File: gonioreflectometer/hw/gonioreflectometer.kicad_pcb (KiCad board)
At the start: 2 copper layers, 25.8 x 20.3 mm, 39 parts, among them J1 Conn_01x07_Pin, J2 Conn_01x07_Pin, Q1 SS8050 200-350, Q10 AO3401A, Q2 SS8050 200-350, Q3 SS8050 200-350, Q4 AO3401A, Q5 AO3400A, Q6 AO3401A, Q7 AO3401A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

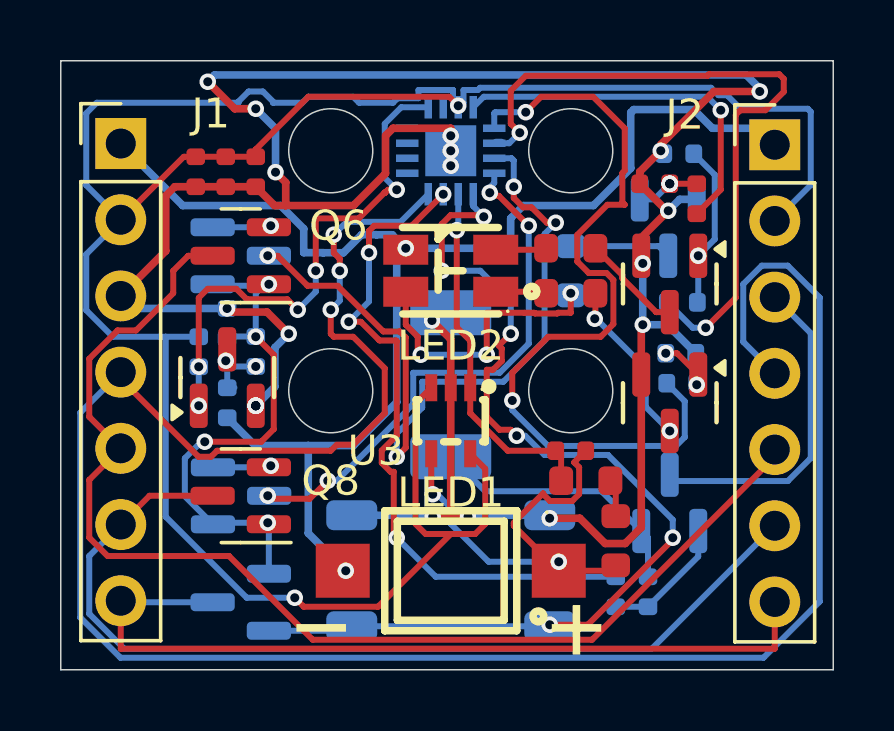
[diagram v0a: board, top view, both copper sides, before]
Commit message: v1.1 fix drc
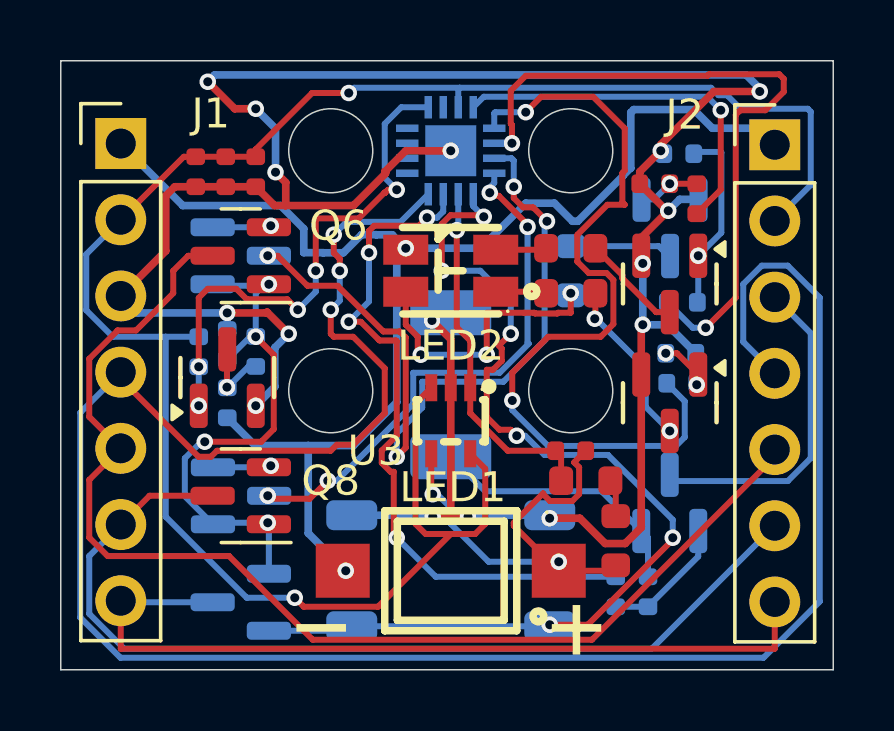
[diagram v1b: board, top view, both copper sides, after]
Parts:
- moved R15 0.70 mm to (75.5, 109.0)
- moved Q3 0.06 mm to (90.3, 105.1)
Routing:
- net 3.3v: track 83.0 -> 65.4 mm
- net GND: track 88.6 -> 87.0 mm, vias 20 -> 16
- net Net-(Q1-B): track 5.48 -> 6.28 mm
- net Net-(Q9-C): track 2.24 -> 2.51 mm, vias 2 -> 1
- net Net-(Q3-B): track 2.12 -> 2.06 mm, vias 2 -> 1

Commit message: v1.1 fix silkscreen on pad
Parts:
- moved R2 0.52 mm to (86.9, 107.8), turned to 15 degrees
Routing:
- net Net-(LED2---Pad3): track 9.38 -> 12.1 mm
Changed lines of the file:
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@@
 			(plot_on_all_layers_selection 0x00000000_00000000_00000000_00000000)
 			(disableapertmacros no)
-			(usegerberextensions no)
+			(usegerberextensions yes)
 			(usegerberattributes yes)
 			(usegerberadvancedattributes yes)
@@
 			(outputformat 1)
 			(mirror no)
-			(drillshape 1)
+			(drillshape 0)
 			(scaleselection 1)
-			(outputdirectory "")
+			(outputdirectory "gerber/")
 		)
 	)
@@
 	(footprint "PCM_JLCPCB:R_0603"
 		(layer "F.Cu")
-		(at 87 107.25)
+		(at 86.93 107.77 15)
 		(descr "Resistor SMD 0603 (1608 Metric), square (rectangular) end terminal, IPC_7351 nominal, (Body size source: IPC-SM-782 page 72, https://www.pcb-3d.com/wordpress/wp-content/uploads/ipc-sm-782a_amendment_1_and_2.pdf), generated with kicad-footprint-generator")
 		(tags "resistor")
 		(property "Reference" "R2"
-			(at 0 -1.3 0)
+			(at 0 -1.3 15)
 			(layer "F.SilkS")
 			(hide yes)
@@
 		)
 		(property "Value" "150Ω"
-			(at 0 1.43 0)
+			(at 0 1.43 15)
 			(layer "F.Fab")
 			(effects
@@
 		)
 		(property "Datasheet" "https://www.lcsc.com/datasheet/lcsc_datasheet_2206010130_UNI-ROYAL-Uniroyal-Elec-0603WAF1500T5E_C22808.pdf"
-			(at 0 0 0)
+			(at 0 0 15)
 			(unlocked yes)
 			(layer "F.Fab")
@@
 		)
 		(property "Description" "100mW Thick Film Resistors 75V ±100ppm/°C ±1% 150Ω 0603 Chip Resistor - Surface Mount ROHS"
-			(at 0 0 0)
+			(at 0 0 15)
 			(unlocked yes)
 			(layer "F.Fab")
@@
 		)
 		(property "LCSC" "C22808"
-			(at 0 0 0)
+			(at 0 0 15)
 			(unlocked yes)
 			(layer "F.Fab")
@@
 		)
 		(property "Stock" "598005"
-			(at 0 0 0)
+			(at 0 0 15)
 			(unlocked yes)
 			(layer "F.Fab")
@@
 		)
 		(property "Price" "0.004USD"
-			(at 0 0 0)
+			(at 0 0 15)
 			(unlocked yes)
 			(layer "F.Fab")
@@
 		)
 		(property "Process" "SMT"
-			(at 0 0 0)
+			(at 0 0 15)
 			(unlocked yes)
 			(layer "F.Fab")
@@
 		)
 		(property "Minimum Qty" "20"
-			(at 0 0 0)
+			(at 0 0 15)
 			(unlocked yes)
 			(layer "F.Fab")
@@
 		)
 		(property "Attrition Qty" "10"
-			(at 0 0 0)
+			(at 0 0 15)
 			(unlocked yes)
 			(layer "F.Fab")
@@
 		)
 		(property "Class" "Basic Component"
-			(at 0 0 0)
+			(at 0 0 15)
 			(unlocked yes)
 			(layer "F.Fab")
@@
 		)
 		(property "Category" "Resistors,Chip Resistor - Surface Mount"
-			(at 0 0 0)
+			(at 0 0 15)
 			(unlocked yes)
 			(layer "F.Fab")
@@
 		)
 		(property "Manufacturer" "UNI-ROYAL(Uniroyal Elec)"
-			(at 0 0 0)
+			(at 0 0 15)
 			(unlocked yes)
 			(layer "F.Fab")
@@
 		)
 		(property "Part" "0603WAF1500T5E"
-			(at 0 0 0)
+			(at 0 0 15)
 			(unlocked yes)
 			(layer "F.Fab")
@@
 		)
 		(property "Resistance" "150Ω"
-			(at 0 0 0)
+			(at 0 0 15)
 			(unlocked yes)
 			(layer "F.Fab")
@@
 		)
 		(property "Power(Watts)" "100mW"
-			(at 0 0 0)
+			(at 0 0 15)
 			(unlocked yes)
 			(layer "F.Fab")
@@
 		)
 		(property "Type" "Thick Film Resistors"
-			(at 0 0 0)
+			(at 0 0 15)
 			(unlocked yes)
 			(layer "F.Fab")
@@
 		)
 		(property "Overload Voltage (Max)" "75V"
-			(at 0 0 0)
+			(at 0 0 15)
 			(unlocked yes)
 			(layer "F.Fab")
@@
 		)
 		(property "Operating Temperature Range" "-55°C~+155°C"
-			(at 0 0 0)
+			(at 0 0 15)
 			(unlocked yes)
 			(layer "F.Fab")
@@
 		)
 		(property "Tolerance" "±1%"
-			(at 0 0 0)
+			(at 0 0 15)
 			(unlocked yes)
 			(layer "F.Fab")
@@
 		)
 		(property "Temperature Coefficient" "±100ppm/°C"
-			(at 0 0 0)
+			(at 0 0 15)
 			(unlocked yes)
 			(layer "F.Fab")
@@
 		)
 		(fp_text user "${REFERENCE}"
-			(at 0 0 0)
+			(at 0 0 15)
 			(layer "F.Fab")
 			(effects
@@
 		)
 		(pad "1" smd roundrect
-			(at -0.82 0)
+			(at -0.82 0 15)
 			(size 0.8 0.95)
 			(layers "F.Cu" "F.Mask" "F.Paste")
@@
 		)
 		(pad "2" smd roundrect
-			(at 0.82 0)
+			(at 0.82 0 15)
 			(size 0.8 0.95)
 			(layers "F.Cu" "F.Mask" "F.Paste")
@@
 	)
 	(segment
-		(start 86.13 107.2)
-		(end 86.18 107.25)
+		(start 85.292232 107.992232)
+		(end 85.302232 107.982232)
 		(width 0.2)
 		(layer "F.Cu")
@@
 	)
 	(segment
-		(start 84.5 107.2)
-		(end 86.13 107.2)
+		(start 85.292232 107.992232)
+		(end 84.5 107.2)
 		(width 0.2)
 		(layer "F.Cu")
@@
 	)
 	(segment
-		(start 87 107.9)
-		(end 87 107.25)
+		(start 85.302232 107.982232)
+		(end 86.137941 107.982232)
 		(width 0.2)
 		(layer "F.Cu")
-		(net "Net-(LED2---Pad3)")
+		(net "Net-(LED2---Pad1)")
 	)
 	(segment
-		(start 81.9 109.2)
-		(end 81.9 108.7)
+		(start 84.2 107.9)
+		(end 83.65 107.9)
 		(width 0.2)
 		(layer "F.Cu")
@@
 	)
 	(segment
-		(start 86.551226 107.925)
-		(end 86.576226 107.9)
+		(start 81.9 109.2)
+		(end 81.9 108.7)
 		(width 0.2)
 		(layer "F.Cu")
@@
 	)
 	(segment
-		(start 86.576226 107.9)
-		(end 87 107.9)
+		(start 81.9 108.7)
+		(end 81.5 108.3)
 		(width 0.2)
 		(layer "F.Cu")
@@
 	)
 	(segment
-		(start 85.808774 107.925)
-		(end 86.551226 107.925)
+		(start 82 109.3)
+		(end 81.9 109.2)
 		(width 0.2)
 		(layer "F.Cu")
@@
 	)
 	(segment
-		(start 84.2 109.3)
-		(end 84.2 107.9)
+		(start 83.55 107.8)
+		(end 83.55 106.5)
 		(width 0.2)
 		(layer "F.Cu")
@@
 	)
 	(segment
-		(start 81.9 108.7)
-		(end 81.5 108.3)
+		(start 83.55 106.5)
+		(end 86.81 106.5)
 		(width 0.2)
 		(layer "F.Cu")
@@
 	)
 	(segment
-		(start 82 109.3)
-		(end 81.9 109.2)
-		(width 0.2)
-		(layer "F.Cu")
-		(net "Net-(LED2---Pad3)")
-	)
-	(segment
-		(start 85.783774 107.9)
-		(end 85.808774 107.925)
+		(start 84.2 109.3)
+		(end 84.2 107.9)
 		(width 0.2)
 		(layer "F.Cu")
@@
 	)
 	(segment
-		(start 84.2 107.9)
-		(end 85.45 107.9)
+		(start 86.81 106.5)
+		(end 86.89 106.58)
 		(width 0.2)
 		(layer "F.Cu")
@@
 	)
 	(segment
-		(start 85.45 107.9)
-		(end 85.783774 107.9)
+		(start 83.65 107.9)
+		(end 83.55 107.8)
 		(width 0.2)
 		(layer "F.Cu")
@@
 	)
 	(via
-		(at 87 107.25)
+		(at 84.2 109.3)
 		(size 0.55)
 		(drill 0.3)
@@
 	)
 	(via
-		(at 84.2 109.3)
+		(at 86.89 106.58)
 		(size 0.55)
 		(drill 0.3)
@@
 	)
 	(segment
+		(start 86.89 106.58)
+		(end 86.89 107.21)
+		(width 0.2)
+		(layer "B.Cu")
+		(net "Net-(LED2---Pad3)")
+	)
+	(segment
+		(start 86.89 107.21)
+		(end 87 107.32)
+		(width 0.2)
+		(layer "B.Cu")
+		(net "Net-(LED2---Pad3)")
+	)
+	(segment
 		(start 77.55 107.45)
 		(end 77.9 107.8)
@@
 		(net "Net-(Q2-B)")
 	)
-	(segment
-		(start 87.82 108.07)
-		(end 87.82 107.25)
-		(width 0.2)
-		(layer "F.Cu")
-		(net "Net-(Q2-C)")
-	)
-	(segment
-		(start 87.8 108.09)
-		(end 87.82 108.07)
-		(width 0.2)
-		(layer "F.Cu")
-		(net "Net-(Q2-C)")
-	)
-	(segment
-		(start 87.8 108.1)
-		(end 87.8 108.09)
-		(width 0.2)
-		(layer "F.Cu")
-		(net "Net-(Q2-C)")
-	)
 	(via
 		(at 90.3 111.84)
@@
 	)
 	(via
-		(at 87.8 108.1)
+		(at 87.89 107.63)
 		(size 0.55)
 		(drill 0.3)
@@
 	)
 	(segment
+		(start 87.89 108.06)
+		(end 87.89 107.63)
+		(width 0.2)
+		(layer "B.Cu")
+		(net "Net-(Q2-C)")
+	)
+	(segment
 		(start 89.5 111.04)
-		(end 90.3 111.84)
+		(end 89.5 109.75)
 		(width 0.2)
 		(layer "B.Cu")
@@
 	)
 	(segment
-		(start 89.5 109.75)
-		(end 89.5 111.04)
+		(start 87.85 108.1)
+		(end 87.89 108.06)
 		(width 0.2)
 		(layer "B.Cu")
@@
 	)
 	(segment
-		(start 87.8 108.1)
+		(start 89.5 109.75)
 		(end 87.85 108.1)
 		(width 0.2)
@@
 	)
 	(segment
-		(start 87.85 108.1)
-		(end 89.5 109.75)
+		(start 90.3 111.84)
+		(end 89.5 111.04)
 		(width 0.2)
 		(layer "B.Cu")

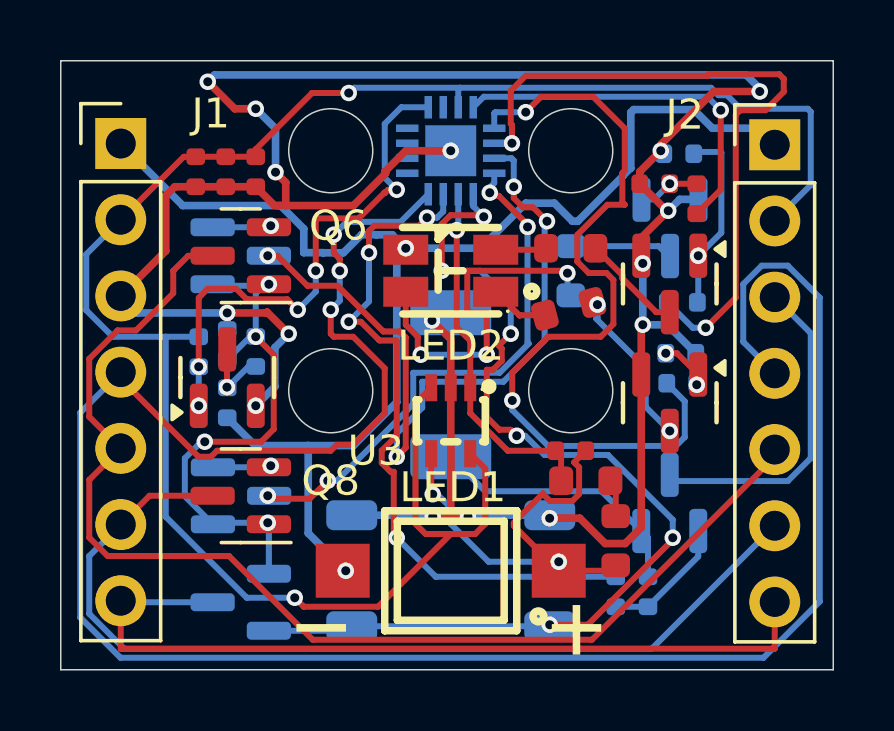
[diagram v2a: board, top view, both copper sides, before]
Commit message: v1.1 minor routing changes
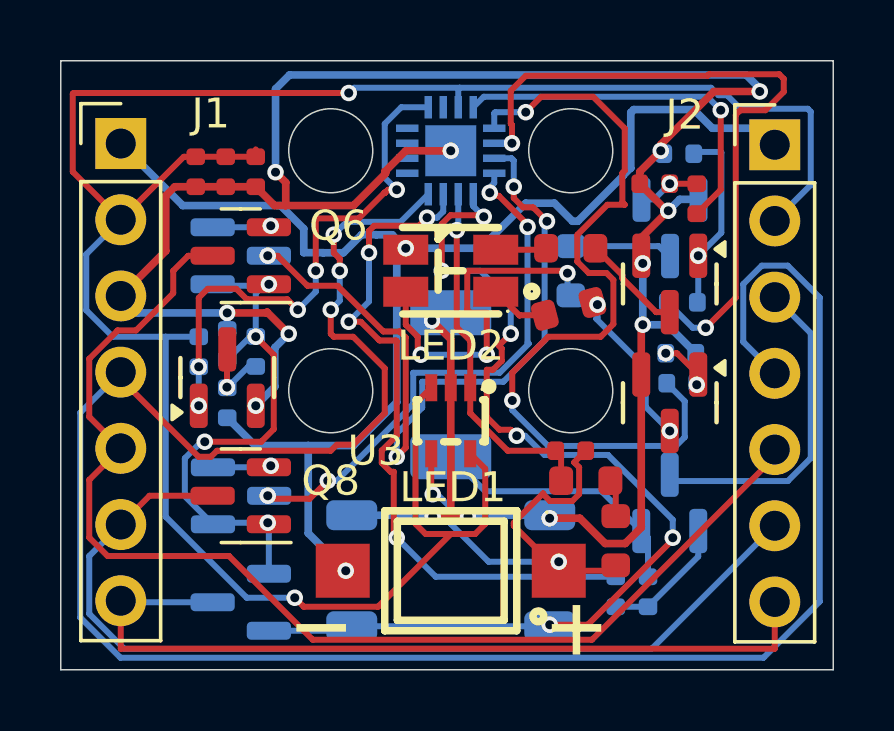
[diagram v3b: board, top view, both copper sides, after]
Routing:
- net 3.3v: track 65.4 -> 75.6 mm
- net GND: track 87.0 -> 83.3 mm, vias 16 -> 14
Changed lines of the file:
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@@
 		(capping no)
 		(filling no)
-		(zone_defaults)
 		(pcbplotparams
 			(layerselection 0x00000000_00000000_55555555_5755f5ff)
@@
 	)
 	(segment
-		(start 75.8 101.1)
-		(end 74.9 100.2)
-		(width 0.254)
-		(layer "F.Cu")
-		(net "GND")
-	)
-	(segment
 		(start 74.5 103.7)
 		(end 75.5 103.7)
@@
 	)
 	(segment
-		(start 76.5 101.1)
-		(end 75.8 101.1)
-		(width 0.254)
-		(layer "F.Cu")
-		(net "GND")
-	)
-	(segment
 		(start 89.35 109.96)
 		(end 89.35 108.35)
@@
 	)
 	(via
-		(at 76.5 101.1)
-		(size 0.55)
-		(drill 0.3)
-		(layers "F.Cu" "B.Cu")
-		(net "GND")
-	)
-	(via
 		(at 77.158941 103.214936)
 		(size 0.55)
@@
 	)
 	(via
-		(at 74.9 100.2)
-		(size 0.55)
-		(drill 0.3)
-		(layers "F.Cu" "B.Cu")
-		(net "GND")
-	)
-	(via
 		(at 90 102.5)
 		(size 0.55)
@@
 	)
 	(segment
-		(start 77.158941 103.214936)
-		(end 77.158941 101.758941)
-		(width 0.254)
-		(layer "B.Cu")
-		(net "GND")
-	)
-	(segment
 		(start 91.167417 109.25)
 		(end 90.217417 108.3)
@@
 	)
 	(segment
-		(start 93.3 100.525)
-		(end 93.3 100.425)
-		(width 0.254)
-		(layer "B.Cu")
-		(net "GND")
-	)
-	(segment
 		(start 91.26 104.13)
 		(end 91.25 104.12)
@@
 	)
 	(segment
-		(start 77.158941 101.758941)
-		(end 76.5 101.1)
+		(start 92.848 99.973)
+		(end 93.3 100.425)
 		(width 0.254)
 		(layer "B.Cu")
@@
 	)
 	(segment
-		(start 90.63 104.12)
-		(end 90.25 104.5)
+		(start 77.627 99.973)
+		(end 92.848 99.973)
 		(width 0.254)
 		(layer "B.Cu")
@@
 	)
 	(segment
-		(start 93.3 100.425)
-		(end 92.848 99.973)
+		(start 77.158941 100.441059)
+		(end 77.627 99.973)
 		(width 0.254)
 		(layer "B.Cu")
@@
 	)
 	(segment
-		(start 92.848 99.973)
-		(end 75.127 99.973)
+		(start 90.63 104.12)
+		(end 90.25 104.5)
 		(width 0.254)
 		(layer "B.Cu")
@@
 	)
 	(segment
-		(start 75.127 99.973)
-		(end 74.9 100.2)
+		(start 93.3 100.425)
+		(end 93.3 100.525)
 		(width 0.254)
 		(layer "B.Cu")
@@
 	)
 	(segment
+		(start 77.158941 103.214936)
+		(end 77.158941 100.441059)
+		(width 0.254)
+		(layer "B.Cu")
+		(net "GND")
+	)
+	(segment
 		(start 90.217417 108.3)
 		(end 89.4 108.3)
@@
 	)
 	(segment
+		(start 70.4 103.2)
+		(end 72 104.8)
+		(width 0.2)
+		(layer "F.Cu")
+		(net "3.3v")
+	)
+	(segment
 		(start 81.825 114.938173)
 		(end 82.161827 115.275)
@@
 	)
 	(segment
-		(start 78.379415 100.575)
-		(end 79.6 100.575)
+		(start 79.6 100.575)
+		(end 70.425 100.575)
 		(width 0.2)
 		(layer "F.Cu")
@@
 	)
 	(segment
+		(start 70.4 100.6)
+		(end 70.4 103.2)
+		(width 0.2)
+		(layer "F.Cu")
+		(net "3.3v")
+	)
+	(segment
 		(start 83 115.275)
 		(end 80.575 117.7)
@@
 	)
 	(segment
-		(start 76.5 102.454415)
-		(end 78.379415 100.575)
-		(width 0.2)
-		(layer "F.Cu")
-		(net "3.3v")
-	)
-	(segment
 		(start 82.35 110.4)
 		(end 81.825 110.925)
@@
 		(width 0.2)
 		(layer "F.Cu")
+		(net "3.3v")
+	)
+	(segment
+		(start 70.425 100.575)
+		(end 70.4 100.6)
+		(width 0.2)
+		(layer "F.Cu")
